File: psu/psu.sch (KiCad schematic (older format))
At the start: 134 parts, among them IC1 ADP3335, IC10 AD8551, IC11 INA139, IC2 TSR 1-2450, IC3 MCP1416, IC4 MCP1416, IC5 STM32F334K8T6, IC6 AD8552, IC7 TSR 1-24150, IC8 BSP772T, IC9 MCP1416, J1 PWR_IN, J2 HV_OUT, J3 CTRL, P1 SWD, Q1 NFET, Q2 NFET, Q3 NFET, X1 HEATSINK, X2 HEATSINK, X3 M3 MOUNT, X4 M3 MOUNT, X5 M3 MOUNT, X6 M3 MOUNT, X7 MAINS PSU, Y1 25M

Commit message: continued updates on psu
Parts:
- removed C1, C2, C3, C4: 100p, symbol agg:C
- removed C10, C11, C15, C9: C, symbol agg:C
- removed C12, C13, C14, C16: CP, symbol agg:CP
- removed C17, C18, C29, C30, C31, C32, C33, C38: 100p, agg:0603, symbol agg:C
- removed C19, C21, C36: 1µ, agg:0805, symbol agg:C
- removed C20, C22, C37: 100n, agg:0603, symbol agg:C
- removed D1, D2: SCHOTTKY, symbol agg:SCHOTTKY
- removed IC10: AD8551, agg:SOIC-8, symbol agg:AD8551
- removed IC11: INA139, agg:SOT-23-5, symbol agg:INA139
- removed IC3, IC4, IC9: MCP1416, agg:SOT-23-5, symbol agg:MCP1416
- removed IC6: AD8552, agg:SOIC-8, symbol agg:AD8552
- removed IC8: BSP772T, agg:SOIC-8, symbol agg:BSP772T
- removed J1: PWR_IN, symbol agg:CONN_01x02
- removed J2: HV_OUT, symbol agg:CONN_01x03
- removed L1, L2: L, symbol agg:L
- removed Q1, Q2, Q3: NFET, symbol agg:NFET
- removed R1, R2, R3, R4: 2R2, symbol agg:R
- removed R10, R18, R25, R41, R43, R44, R50, R7: 100k, agg:0603, symbol agg:R
- removed R11, R12, R40, R8, R9: 100m, agg:1210, symbol agg:R
- removed R13, R14, R15, R19, R20, R29, R34: 500k, agg:0805, symbol agg:R
- removed R21, R33: 10k, agg:0603, symbol agg:R
- removed R22, R23: 10k, agg:0805, symbol agg:R
- removed R24: 20k, agg:0603, symbol agg:R
- removed R26, R27, R45: 1k, agg:0603, symbol agg:R
- removed R28: 10m, agg:1210, symbol agg:R
- removed R30, R35, R36, R39: 100, agg:0805, symbol agg:R
- removed R5, R6: 1k, agg:0805, symbol agg:R
- removed TP1, TP2: TESTPAD, agg:TESTPAD, symbol agg:TESTPAD
- removed X1, X2: HEATSINK, symbol agg:PART
- added C?: 100p, agg:0603, symbol agg:C
- added J?: HV_OUT, symbol agg:CONN_01x03
- added J?: PWR_IN, symbol agg:BarrelJack
- added R?: 100k, agg:0603, symbol agg:R
- added R?: 10k, agg:0603, symbol agg:R
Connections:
- net labels added: I_24V, I_400V, I_L1, I_L2
- net labels removed: 100V, 24VRS+, 24VRS-, 400V, VRS1, VRS1A, VRS2, VRS2A, VRS3, VRS3A, VRS4A
- wire segments 416 -> 197
- no-connect marks 6 -> 7
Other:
- note added: "High-Voltage Boost Converter"
- note added: "Low-Voltage Regulators"
- note added: "Power Input"
- note removed: "100V 500mA"
- note removed: "100V in\n1.96V out\n19mW"
- note removed: "24V 2.5A"
- note removed: "400V 100mA"
- note removed: "400V in\n1.99V out\n80mW"
- note removed: "Active Discharge\nGate Driver"
- note removed: "Active discharge"
- note removed: "Current Sense Amplifiers"
- note removed: "Current sense resistor:\nImax 0.5A\n0.5A*50mR=0.025V\n12.5mW, 6mW per R"
- note removed: "Current sense resistor:\nImax 2.5A\n2.5A*50mR=0.125V\n312mW, 156mW per R"
- note removed: "Feedback Voltage Dividers"
- note removed: "First Stage\nGate Driver"
- note removed: "High-Side Power Switch"
- note removed: "High-Voltage\nBoost Converter"
- note removed: "Passive discharge\nin ~~300s"
- note removed: "Power Input and Low-Voltage Regulators"
- note removed: "Second Stage\nGate Driver"
- note removed: "Snubber"
- note removed: "VRS1A = (1+R2/R1)VRS1\n= 21 * I_L1 * 0.05\n= 2.625V at 2.5A"
- note removed: "VRS2A = (1+R2/R1)VRS2\n= 101 * I_L2 * 0.05\n= 2.525V at 500mA"
- note removed: "VRS3A = (1+R2/R1)VRS3\n= 201 * Iout * 0.1\n= 2.01V at 100mA"
- note removed: "VRS4A = 24VRS * R1/1k\n= I_24V\n= 2.5V at 2.5A"
- moved on the sheet: C23, C24, C25, C26, C27, C28, C34, C35, C5, C6, C7, C8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

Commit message: update psu
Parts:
- gave numbers to parts that had none: 5
- renumbered C35 to C1, C25 to C10, C26 to C11, C27 to C12, C28 to C13, C34 to C2, C5 to C3, C6 to C4, C7 to C5, C8 to C6, C23 to C8, C24 to C9, D6 to D1, D12 to D10, D13 to D11, D14 to D12, D15 to D13, D7 to D2, D10 to D3, D9 to D4, D11 to D5, D8 to D6, D3 to D7, D4 to D8, D5 to D9, IC7 to IC2, IC2 to IC3, IC5 to IC4, L3 to L1, R46 to R10, R47 to R11, R48 to R12, R49 to R13, R37 to R3, R32 to R4, R38 to R5, R31 to R6, R42 to R7, R16 to R8, R17 to R9, X3 to X1, X4 to X2, X5 to X3, X6 to X4, X7 to X5
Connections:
- net LED_FAULT: now also IC4.30 (PB7); no longer IC4.25 (PA15)
- net ~RUN: now also IC4.25 (PA15); no longer IC4.30 (PB7)
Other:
- note added: "24V in, 15V 1A out"
- note added: "24V in, 5V 1A out"
- note added: "5V in, 3.3V 0.5A out"
- note added: "PA0: ADC1_C1"
- note added: "PA10: TIM1_C3, HRTIM1_CB1"
- note added: "PA15: TIM1_BKIN, HRTIM1_FLT2"
- note added: "PA1: ADC1_C2"
- note added: "PA2: ADC1_C3"
- note added: "PA3: ADC1_C4"
- note added: "PA5: ADC2_C2"
- note added: "PA6: ADC2_C3"
- note added: "PA7: ADC2_C4, COMP2_IN+"
- note added: "PA8: TIM1_C1, HRTIM1_CA1"
- note added: "PA9: GPIO, TIM2_C3"
- note added: "PB0: COMP4_IN+"
- note added: "PB1: TIM3_C4"
- note removed: "24Vin 15Vout 1Aout"
- note removed: "24Vin 5Vout 1Aout"
- note removed: "5Vin 3.3Vout 0.5Aout"
- note removed: "PA0: ADC1C1"
- note removed: "PA10: TIM1C3, HRTIM1CB1"
- note removed: "PA1: ADC1C2"
- note removed: "PA2: ADC1C3"
- note removed: "PA3: ADC1C4"
- note removed: "PA5: ADC2C2"
- note removed: "PA6: ADC2C3"
- note removed: "PA7: ADC2C4, COMP2IN+"
- note removed: "PA8: TIM1C1, HRTIM1CA1"
- note removed: "PA9: GPIO, TIM2C3"
- note removed: "PB0: COMP4IN+"
- note removed: "PB1: TIM3C4"
- moved on the sheet: C10, C11, C12, C13, C8, C9, D10, D11, D12, D13, IC4, L1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

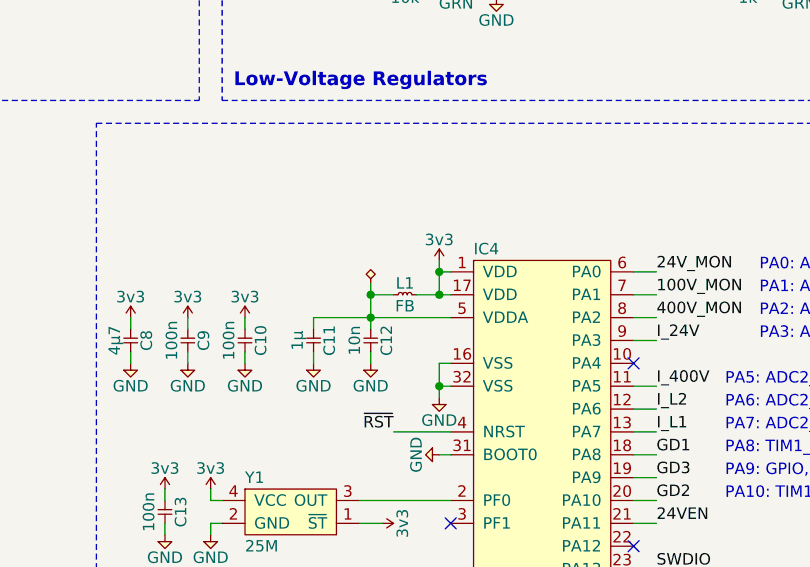
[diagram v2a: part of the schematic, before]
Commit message: assign diodes and main transistors
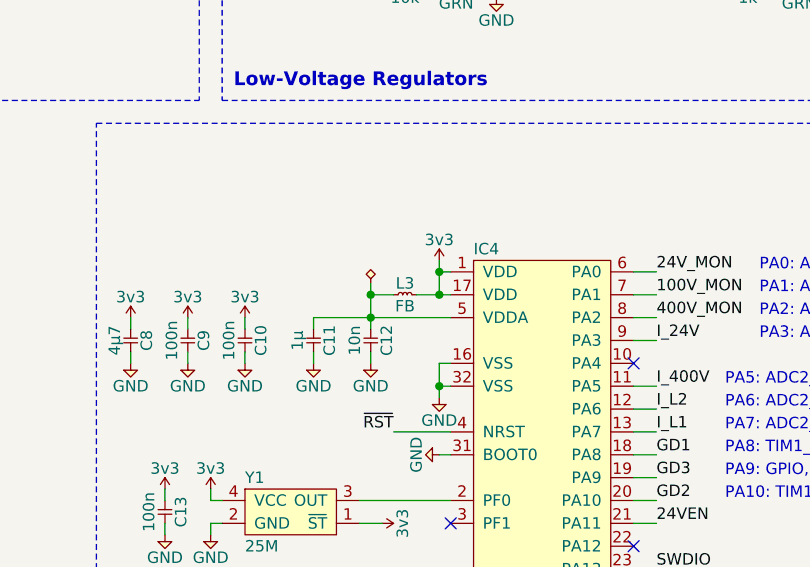
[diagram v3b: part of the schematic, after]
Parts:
- renumbered L1 to L3
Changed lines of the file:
@@
 	4100 3250 4100 3350
 $Comp
-L agg:L L1
+L agg:L L3
 U 1 1 5D480F40
 P 3900 3350
-F 0 "L1" H 3950 3400 50  0000 C CNN
+F 0 "L3" H 3950 3400 50  0000 C CNN
 F 1 "FB" H 3950 3300 50  0000 C CNN
 F 2 "agg:0603" H 3900 3350 50  0001 C CNN

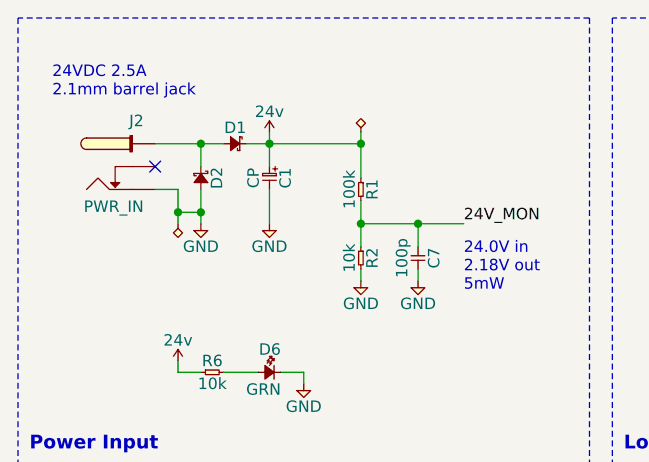
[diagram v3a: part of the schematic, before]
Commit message: Select main L and C
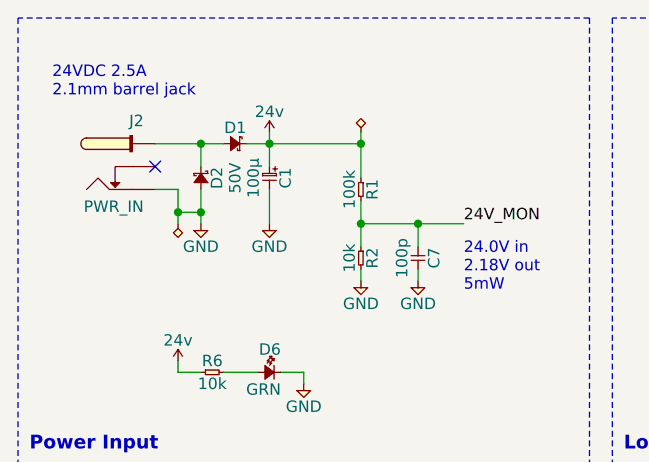
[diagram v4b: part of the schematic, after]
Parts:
- C1: value CP -> 100µ; Farnell (none) -> 2079271; Voltage 50 -> 50V
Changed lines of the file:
@@
 Text Label 5050 4150 0    50   ~ 0
 GD3
-$Comp
-L agg:CP C1
-U 1 1 6036C0A4
-P 1650 1300
-F 0 "C1" H 1700 1370 50  0000 C CNN
-F 1 "CP" H 1700 1230 50  0000 C CNN
-F 2 "" H 1650 1300 50  0001 C CNN
-F 3 "" H 1650 1300 50  0001 C CNN
-F 4 "50" H 1650 1300 50  0001 C CNN "Voltage"
-	1    1650 1300
-	0    1    -1   0
-$EndComp
 Wire Wire Line
 	1650 1200 1650 1100
@@
 Text Notes 5350 4750 0    50   ~ 0
 PA15: TIM1_BKIN, HRTIM1_FLT2
+$Comp
+L agg:CP C1
+U 1 1 62DF485C
+P 1650 1300
+AR Path="/62DF485C" Ref="C1"  Part="1"
+AR Path="/6147A5D5/62DF485C" Ref="C?"  Part="1"
+F 0 "C1" H 1700 1370 50  0000 C CNN
+F 1 "100µ" H 1700 1230 50  0000 C CNN
+F 2 "" H 1650 1300 50  0001 C CNN
+F 3 "http://industrial.panasonic.com/cdbs/www-data/pdf/RDE0000/ABA0000C1187.pdf" H 1650 1300 50  0001 C CNN
+F 4 "50V" H 1700 1150 50  0000 C CNN "Voltage"
+F 5 "2079271" H 1650 1300 50  0001 C CNN "Farnell"
+	1    1650 1300
+	0    1    -1   0
+$EndComp
 $EndSCHEMATC

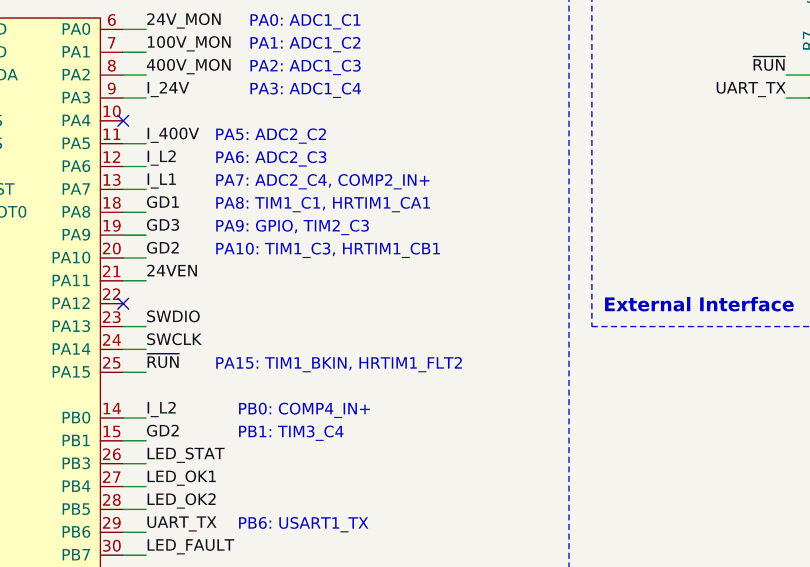
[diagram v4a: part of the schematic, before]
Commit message: Update current sense Rs
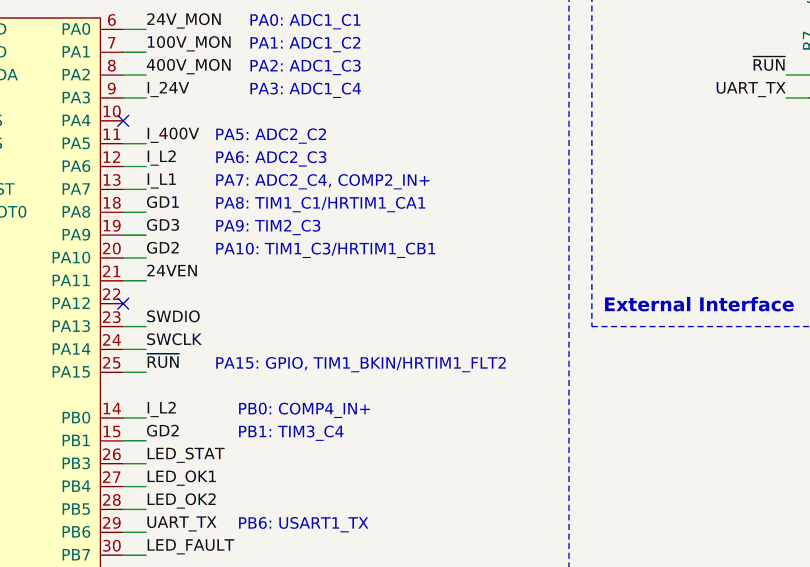
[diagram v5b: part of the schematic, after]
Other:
- note added: "PA10: TIM1_C3/HRTIM1_CB1"
- note added: "PA15: GPIO, TIM1_BKIN/HRTIM1_FLT2"
- note added: "PA8: TIM1_C1/HRTIM1_CA1"
- note added: "PA9: TIM2_C3"
- note removed: "PA10: TIM1_C3, HRTIM1_CB1"
- note removed: "PA15: TIM1_BKIN, HRTIM1_FLT2"
- note removed: "PA8: TIM1_C1, HRTIM1_CA1"
- note removed: "PA9: GPIO, TIM2_C3"
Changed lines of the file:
@@
 	5050 4050 4950 4050
 Text Notes 5350 4050 0    50   ~ 0
-PA8: TIM1_C1, HRTIM1_CA1
+PA8: TIM1_C1/HRTIM1_CA1
 Wire Wire Line
 	5050 4250 4950 4250
 Text Notes 5350 4250 0    50   ~ 0
-PA10: TIM1_C3, HRTIM1_CB1
+PA10: TIM1_C3/HRTIM1_CB1
 $Comp
 L agg:SCHOTTKY D1
@@
 	5050 4150 4950 4150
 Text Notes 5350 4150 0    50   ~ 0
-PA9: GPIO, TIM2_C3
+PA9: TIM2_C3
 Wire Wire Line
 	5050 4350 4950 4350
@@
 NoConn ~ 1150 1200
 Text Notes 5350 4750 0    50   ~ 0
-PA15: TIM1_BKIN, HRTIM1_FLT2
+PA15: GPIO, TIM1_BKIN/HRTIM1_FLT2
 $Comp
 L agg:CP C1

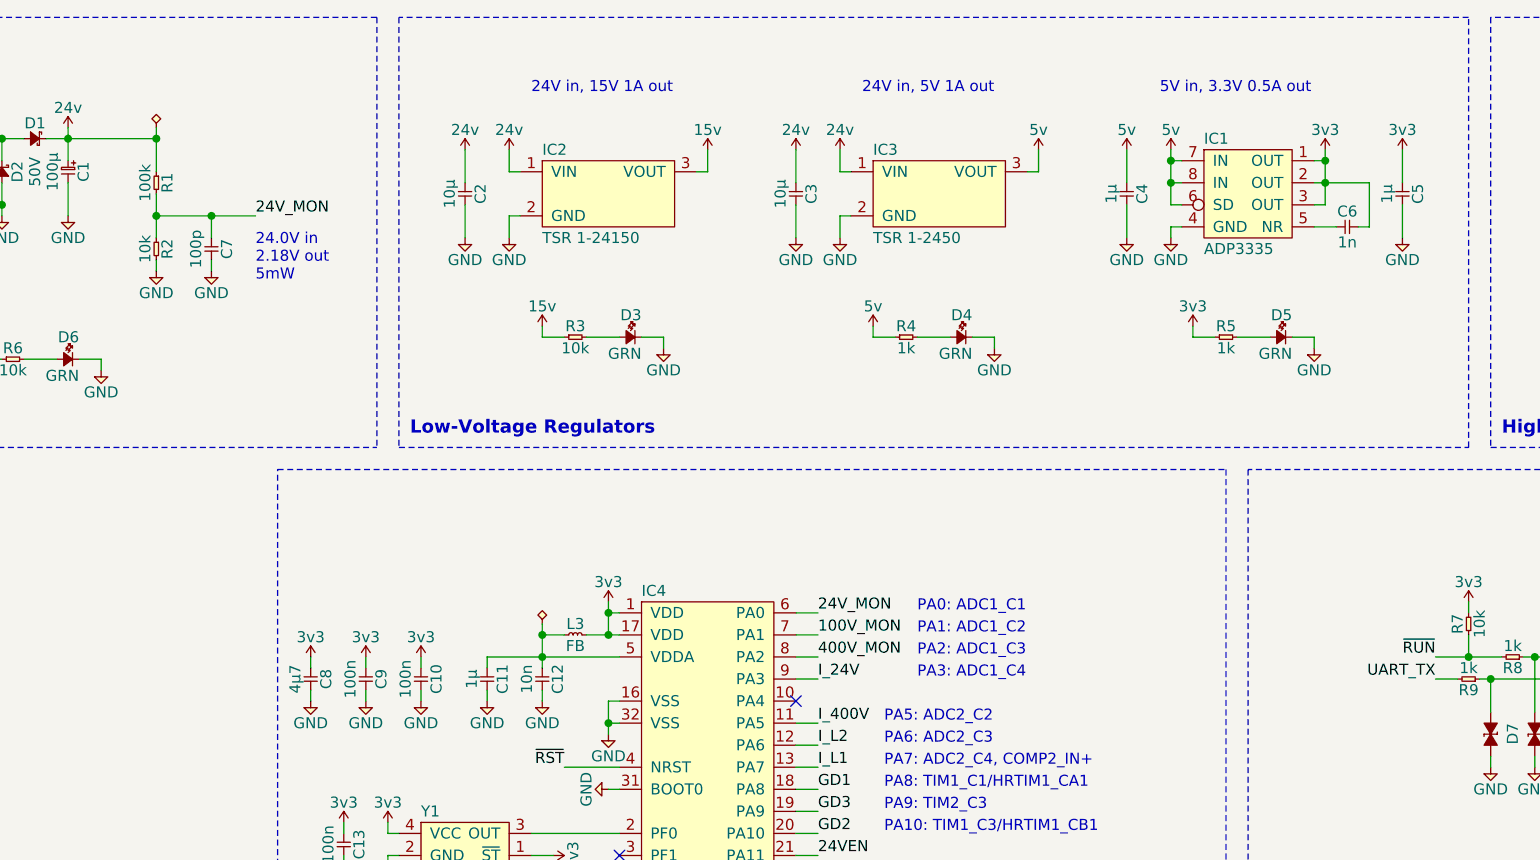
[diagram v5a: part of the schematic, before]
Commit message: update before swapping to flyback
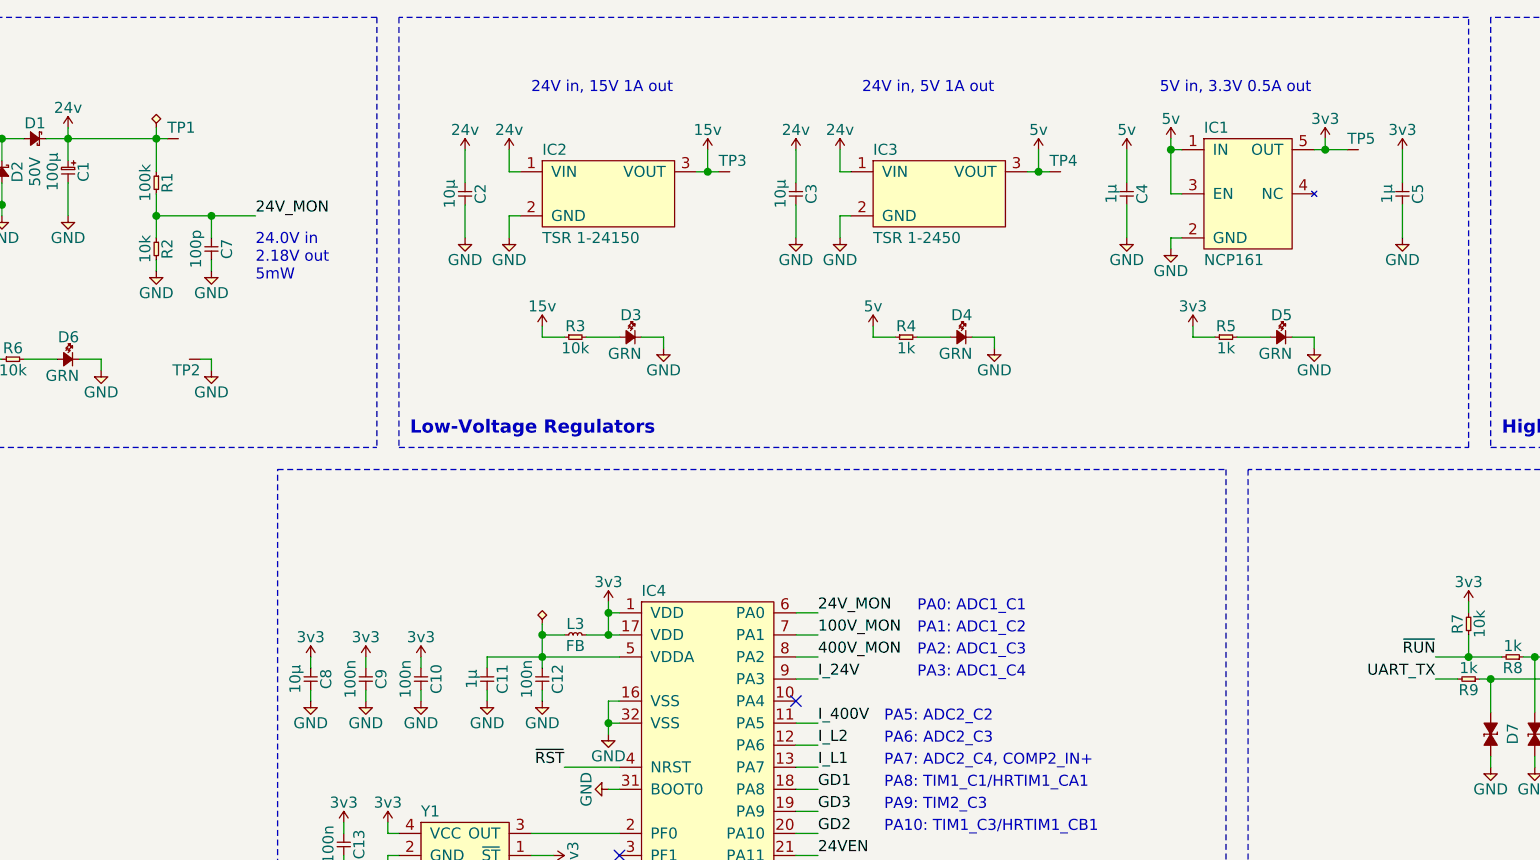
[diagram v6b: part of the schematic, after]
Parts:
- removed C6: 1n, agg:0603, symbol agg:C
- removed IC1: ADP3335, agg:MSOP-8, symbol agg:ADP3335
- added IC1: NCP161, agg:SOT-23-5, symbol agg:NCP161
- added TP1, TP3, TP4, TP5: TESTPAD, agg:TESTPAD, symbol agg:TESTPAD
- added TP2: TESTPAD, agg:SIL-254P-01, symbol agg:TESTPAD
- C1: footprint (none) -> agg:PANASONIC-SMDCAP-G
- C10, C13, C9: Farnell (none) -> 2320803; Voltage 50 -> 50V
- C11, C4, C5: Farnell (none) -> 2320814; Voltage 16 -> 16V
- C12: value 10n -> 100n; Farnell (none) -> 2320803; Voltage 50 -> 50V
- C2, C3: footprint agg:1206 -> agg:1210; Farnell (none) -> 2781426; Voltage 50 -> 50V
- C7: Farnell (none) -> 9406115; Voltage 50 -> 50V
- C8: value 4µ7 -> 10µ; footprint agg:0603 -> agg:1210; Farnell (none) -> 2781426; Voltage 16 -> 50V
- D1: footprint aggl:DO-214AB-SMC -> agg:DO-214AB-SMC
- D7, D8, D9: Voltage 24 -> 24V
- IC2: Farnell (none) -> 1672131
- IC3: Farnell (none) -> 1696320
- J1: footprint (none) -> agg:MOLEX-KK-254P-03; Farnell (none) -> 1360131
- J2: footprint (none) -> agg:BARRELJACK
- J3: footprint (none) -> agg:MOLEX-KK-254P-04; Farnell (none) -> 1360132
- L3: Farnell (none) -> 1515747
- P1: footprint agg:FTSH-105-01-F-D-K -> agg:FTSH-105-01-L-DV-K; Farnell (none) -> 2856437
- R1: Farnell (none) -> 2447226; Voltage (none) -> 50V
- R10, R11, R12, R13, R4, R5, R8, R9: Farnell (none) -> 2447272; Voltage (none) -> 50V
- R2, R3, R6, R7: Farnell (none) -> 2447230; Voltage (none) -> 50V
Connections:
- net 15v: now also TP3.1 (TP)
- net 24v: now also TP1.1 (TP)
- net 3v3: now also IC1.5 (OUT), TP5.1 (TP)
- net 5v: now also IC1.1 (IN), IC1.3 (EN), TP4.1 (TP)
- net GND: now also IC1.2 (GND), TP2.1 (TP)
